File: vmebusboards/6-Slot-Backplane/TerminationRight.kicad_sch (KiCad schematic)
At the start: 25 parts, among them U4 OPAMP_8-pin_Generic

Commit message: Updated
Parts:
- added C23: 0.1uF, symbol Device:C_Small
- added C24: 4.7uF, Capacitor_THT:CP_Radial_D5.0mm_P2.00mm, symbol Device:C_Polarized_Small_US
- added JP7, JP8: PASSIVE/ACTIVE, Connector_PinHeader_2.54mm:PinHeader_1x02_P2.54mm_Vertical, symbol Jumper:Jumper_3_Bridged12
- added R21: 330, symbol Device:R_Small
- added R22: 470, symbol Device:R_Small
- added unit 2 of U2
- C22: renamed from C20; footprint (none) -> Capacitor_THT:CP_Radial_D5.0mm_P2.00mm
- JP5: renamed from JP3; footprint (none) -> Connector_PinHeader_2.54mm:PinHeader_1x02_P2.54mm_Vertical
- JP6: renamed from JP4; footprint (none) -> Connector_PinHeader_2.54mm:PinHeader_1x02_P2.54mm_Vertical
- RN13, RN14, RN15, RN16, RN17, RN18, RN19, RN20, RN21, RN22, RN23, RN24: symbol Computie_Transceivers:R_Network_Dividers_x08_SIP_Small -> Computie_Miscellaneous:R_Network_Dividers_x08_SIP_Small
- renumbered C15 to C17, C16 to C18, C17 to C19, C18 to C20, C19 to C21, U4 to U2
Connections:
- net +5V: now also C23.1, JP7.1 (A), R21.1
- net GND: now also C23.2, C24.2, JP8.1 (A), R22.2
- net TERM0_HIGH renamed TERM_R1_HIGH
- net TERM_R1_HIGH: now also RN13.10 (COM2), RN14.10 (COM2), RN15.10 (COM2), RN16.10 (COM2), RN17.10 (COM2)
- net TERM0_LOW renamed TERM_R1_LOW
- net TERM_R1_LOW: now also RN13.1 (COM1), RN14.1 (COM1), RN15.1 (COM1), RN16.1 (COM1), RN17.1 (COM1)
- net TERM1_HIGH renamed TERM_R2_HIGH
- net TERM_R2_HIGH: now also R5.2, JP7.2 (C); no longer RN17.10 (COM2)
- net TERM1_LOW renamed TERM_R2_LOW
- net TERM_R2_LOW: now also R6.1, JP8.2 (C); no longer RN17.1 (COM1)
- removed net TERM2_HIGH: R5.2, RN13.10 (COM2), RN14.10 (COM2), RN15.10 (COM2), RN16.10 (COM2)
- removed net TERM2_LOW: R6.1, RN13.1 (COM1), RN14.1 (COM1), RN15.1 (COM1), RN16.1 (COM1)
- new net: R21.2, R22.1, U2.6 (-)
- new net: C24.1, JP7.3 (B), JP8.3 (B), U2.5 (+), U2.7
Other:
- note removed: "NOTE: the standard says SERCLK and SERDATA are not required to have resistor networks, but the backplane I have pulls them up to 3V so not sure what to do for them"

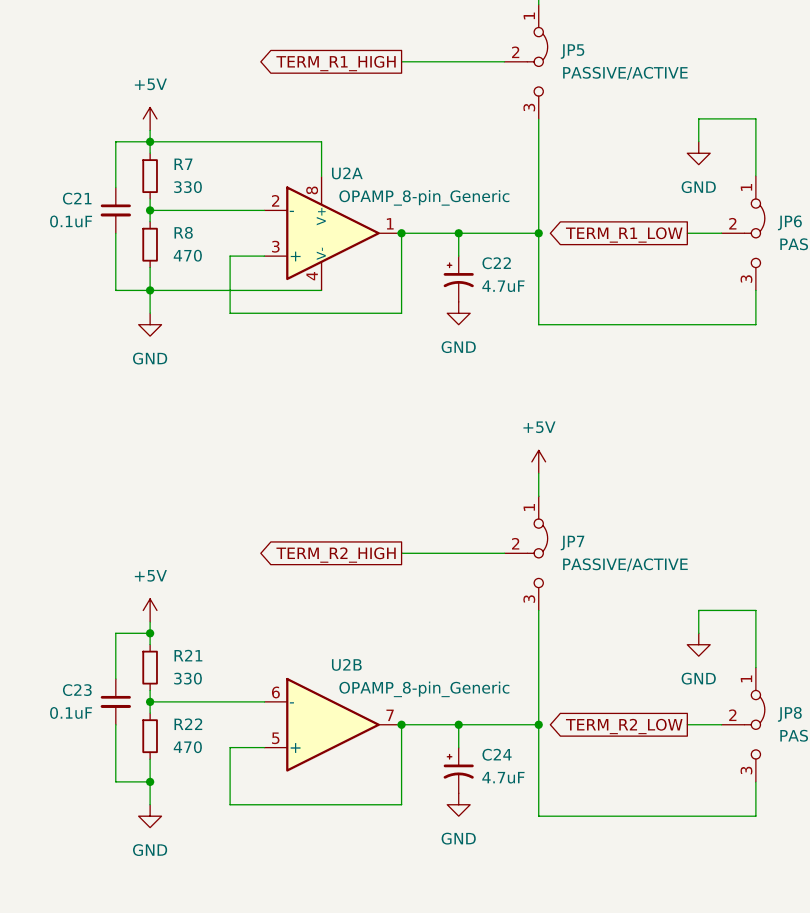
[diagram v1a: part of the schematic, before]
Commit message: Added SystemBoardSMT, renamed k30 boards, and added progress
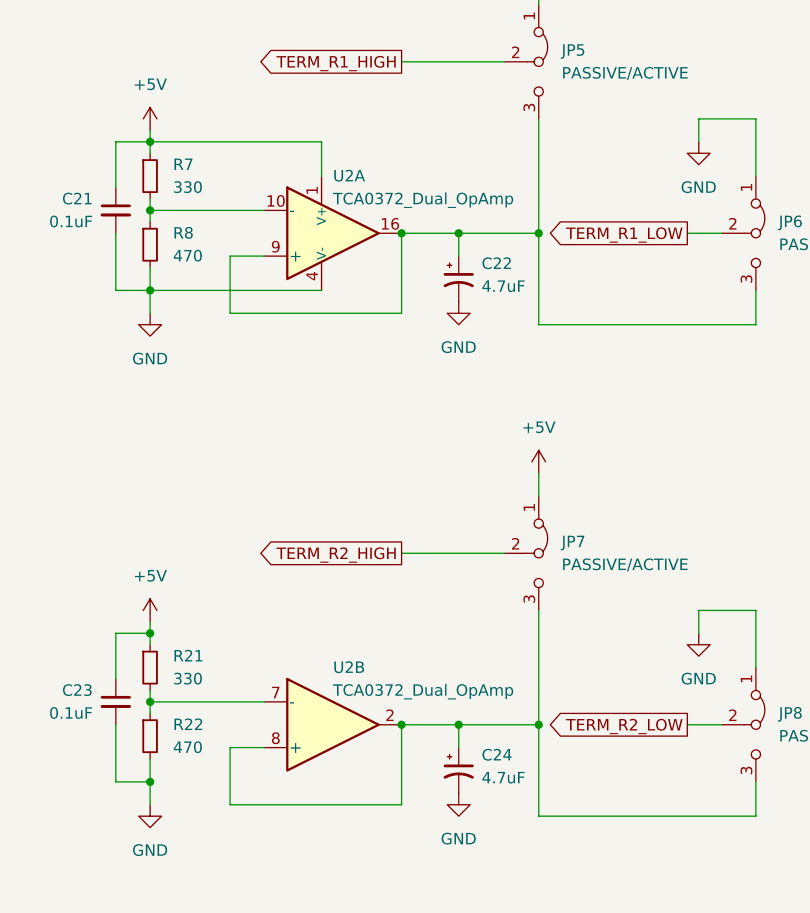
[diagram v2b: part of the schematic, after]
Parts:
- R21, R22, R5, R6, R7, R8: footprint (none) -> Resistor_SMD:R_0805_2012Metric_Pad1.20x1.40mm_HandSolder
- RN13, RN14, RN15, RN16, RN17, RN18, RN19, RN20, RN21, RN22, RN23, RN24: footprint Resistor_THT:R_Array_SIP10 -> Connector_PinHeader_2.54mm:PinHeader_1x10_P2.54mm_Vertical
- U2: value OPAMP_8-pin_Generic -> TCA0372_Dual_OpAmp; footprint (none) -> Package_SO:SOIC-16W_7.5x10.3mm_P1.27mm; symbol PCM_Amplifier_Operational_AKL:OPAMP_Dual_Generic -> Computie_Miscellaneous:TCA0372_Dual_OpAmp
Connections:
- net +5V: now also U2.1 (V+); no longer U2.8 (V+)
- net GND: now also U2.12 (V-), U2.13 (V-), U2.5 (V-)
- net at R21.2, R22.1: now also U2.7 (-); no longer U2.6 (-)
- net at C22.1, JP5.3 (B), JP6.3 (B): now also U2.16, U2.9 (+); no longer U2.1, U2.3 (+)
- net at C24.1, JP7.3 (B), JP8.3 (B): now also U2.2, U2.8 (+); no longer U2.5 (+), U2.7
- net at R7.2, R8.1: now also U2.10 (-); no longer U2.2 (-)
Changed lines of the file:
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@@
 			)
 		)
-		(property "Footprint" ""
+		(property "Footprint" "Resistor_SMD:R_0805_2012Metric_Pad1.20x1.40mm_HandSolder"
 			(at 198.12 107.95 0)
 			(effects
@@
 			)
 		)
-		(property "Footprint" "Resistor_THT:R_Array_SIP10"
+		(property "Footprint" "Connector_PinHeader_2.54mm:PinHeader_1x10_P2.54mm_Vertical"
 			(at 96.52 153.035 90)
 			(effects
@@
 			)
 		)
-		(property "Footprint" "Resistor_THT:R_Array_SIP10"
+		(property "Footprint" "Connector_PinHeader_2.54mm:PinHeader_1x10_P2.54mm_Vertical"
 			(at 96.52 57.785 90)
 			(effects
@@
 	)
 	(symbol
-		(lib_id "PCM_Amplifier_Operational_AKL:OPAMP_Dual_Generic")
+		(lib_id "Computie_Miscellaneous:TCA0372_Dual_OpAmp")
 		(at 217.17 59.69 0)
 		(unit 1)
@@
 		(dnp no)
 		(property "Reference" "U2"
-			(at 219.964 53.086 0)
+			(at 218.44 53.34 0)
 			(effects
 				(font
 					(size 1.27 1.27)
 				)
+				(justify left)
 			)
 		)
-		(property "Value" "OPAMP_8-pin_Generic"
-			(at 228.6 55.626 0)
+		(property "Value" "TCA0372_Dual_OpAmp"
+			(at 218.44 55.88 0)
 			(effects
 				(font
 					(size 1.27 1.27)
 				)
+				(justify left)
 			)
 		)
-		(property "Footprint" ""
+		(property "Footprint" "Package_SO:SOIC-16W_7.5x10.3mm_P1.27mm"
 			(at 217.17 59.69 0)
 			(effects
@@
 		(pin "2"
 		)
-		(pin "3"
+		(pin "10"
 		)
 		(pin "8"
 		)
-		(pin "6"
+		(pin "13"
 		)
 		(pin "4"
@@
 		(pin "1"
 		)
+		(pin "12"
+		)
+		(pin "16"
+		)
+		(pin "9"
+		)
 		(instances
 			(project "6-Slot-Backplane"
@@
 			)
 		)
-		(property "Footprint" ""
+		(property "Footprint" "Resistor_SMD:R_0805_2012Metric_Pad1.20x1.40mm_HandSolder"
 			(at 198.12 60.96 0)
 			(effects
@@
 			)
 		)
-		(property "Footprint" ""
+		(property "Footprint" "Resistor_SMD:R_0805_2012Metric_Pad1.20x1.40mm_HandSolder"
 			(at 41.91 162.56 0)
 			(effects
@@
 			)
 		)
-		(property "Footprint" "Resistor_THT:R_Array_SIP10"
+		(property "Footprint" "Connector_PinHeader_2.54mm:PinHeader_1x10_P2.54mm_Vertical"
 			(at 153.67 121.285 90)
 			(effects
@@
 			)
 		)
-		(property "Footprint" "Resistor_THT:R_Array_SIP10"
+		(property "Footprint" "Connector_PinHeader_2.54mm:PinHeader_1x10_P2.54mm_Vertical"
 			(at 39.37 121.285 90)
 			(effects
@@
 			)
 		)
-		(property "Footprint" "Resistor_THT:R_Array_SIP10"
+		(property "Footprint" "Connector_PinHeader_2.54mm:PinHeader_1x10_P2.54mm_Vertical"
 			(at 153.67 89.535 90)
 			(effects
@@
 			)
 		)
-		(property "Footprint" "Resistor_THT:R_Array_SIP10"
+		(property "Footprint" "Connector_PinHeader_2.54mm:PinHeader_1x10_P2.54mm_Vertical"
 			(at 153.67 57.785 90)
 			(effects
@@
 			)
 		)
-		(property "Footprint" "Resistor_THT:R_Array_SIP10"
+		(property "Footprint" "Connector_PinHeader_2.54mm:PinHeader_1x10_P2.54mm_Vertical"
 			(at 39.37 89.535 90)
 			(effects
@@
 			)
 		)
-		(property "Footprint" "Resistor_THT:R_Array_SIP10"
+		(property "Footprint" "Connector_PinHeader_2.54mm:PinHeader_1x10_P2.54mm_Vertical"
 			(at 39.37 153.035 90)
 			(effects
@@
 			)
 		)
-		(property "Footprint" "Resistor_THT:R_Array_SIP10"
+		(property "Footprint" "Connector_PinHeader_2.54mm:PinHeader_1x10_P2.54mm_Vertical"
 			(at 39.37 57.785 90)
 			(effects
@@
 			)
 		)
-		(property "Footprint" "Resistor_THT:R_Array_SIP10"
+		(property "Footprint" "Connector_PinHeader_2.54mm:PinHeader_1x10_P2.54mm_Vertical"
 			(at 96.52 121.285 90)
 			(effects
@@
 			)
 		)
-		(property "Footprint" ""
+		(property "Footprint" "Resistor_SMD:R_0805_2012Metric_Pad1.20x1.40mm_HandSolder"
 			(at 198.12 115.57 0)
 			(effects
@@
 			)
 		)
-		(property "Footprint" "Resistor_THT:R_Array_SIP10"
+		(property "Footprint" "Connector_PinHeader_2.54mm:PinHeader_1x10_P2.54mm_Vertical"
 			(at 153.67 153.035 90)
 			(effects
@@
 			)
 		)
-		(property "Footprint" "Resistor_THT:R_Array_SIP10"
+		(property "Footprint" "Connector_PinHeader_2.54mm:PinHeader_1x10_P2.54mm_Vertical"
 			(at 96.52 89.535 90)
 			(effects
@@
 			)
 		)
-		(property "Footprint" ""
+		(property "Footprint" "Resistor_SMD:R_0805_2012Metric_Pad1.20x1.40mm_HandSolder"
 			(at 198.12 53.34 0)
 			(effects
@@
 			)
 		)
-		(property "Footprint" ""
+		(property "Footprint" "Resistor_SMD:R_0805_2012Metric_Pad1.20x1.40mm_HandSolder"
 			(at 36.83 165.1 0)
 			(effects
@@
 	)
 	(symbol
-		(lib_id "PCM_Amplifier_Operational_AKL:OPAMP_Dual_Generic")
+		(lib_id "Computie_Miscellaneous:TCA0372_Dual_OpAmp")
 		(at 217.17 114.3 0)
 		(unit 2)
@@
 		(dnp no)
 		(property "Reference" "U2"
-			(at 219.964 107.696 0)
+			(at 218.44 107.95 0)
 			(effects
 				(font
 					(size 1.27 1.27)
 				)
+				(justify left)
 			)
 		)
-		(property "Value" "OPAMP_8-pin_Generic"
-			(at 228.6 110.236 0)
+		(property "Value" "TCA0372_Dual_OpAmp"
+			(at 218.44 110.49 0)
 			(effects
 				(font
 					(size 1.27 1.27)
 				)
+				(justify left)
 			)
 		)
-		(property "Footprint" ""
+		(property "Footprint" "Package_SO:SOIC-16W_7.5x10.3mm_P1.27mm"
 			(at 217.17 114.3 0)
 			(effects
@@
 		(pin "2"
 		)
-		(pin "3"
+		(pin "10"
 		)
 		(pin "8"
 		)
-		(pin "6"
+		(pin "13"
 		)
 		(pin "4"
@@
 		(pin "1"
 		)
+		(pin "16"
+		)
+		(pin "9"
+		)
+		(pin "12"
+		)
 		(instances
